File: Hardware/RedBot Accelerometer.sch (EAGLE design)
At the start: 18 parts, among them U1 MMA8452Q, U2 MIC5205-3.3V, U3 PCA9306

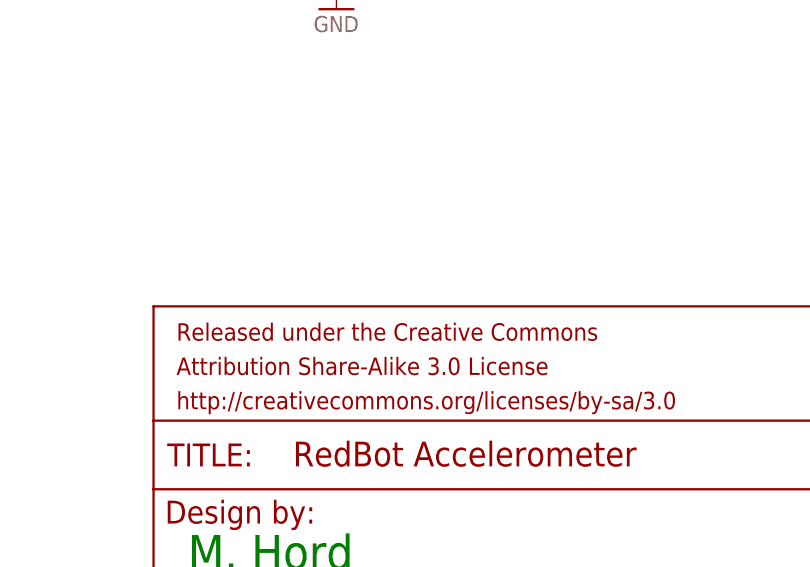
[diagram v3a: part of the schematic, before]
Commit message: added fiducials to board
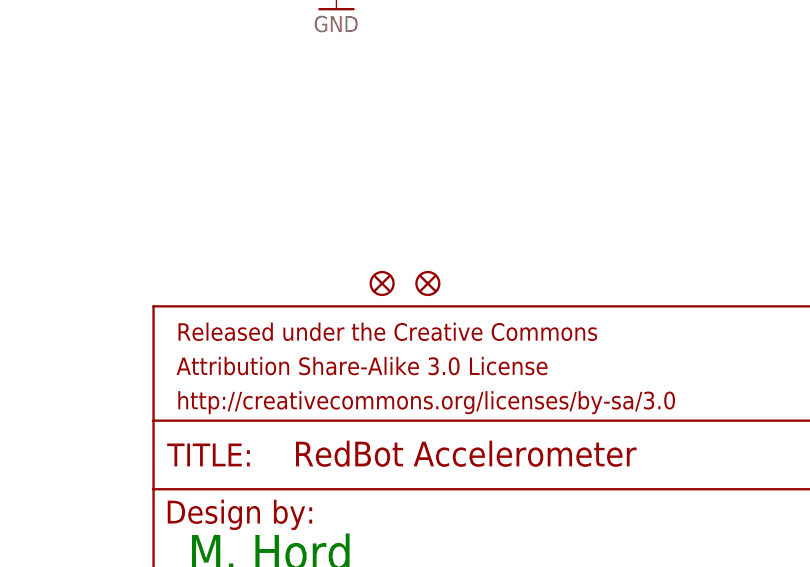
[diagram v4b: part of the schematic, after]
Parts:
- added FID1, FID2: FIDUCIALUFIDUCIAL, SparkFun-Aesthetics:FIDUCIALUFIDUCIAL
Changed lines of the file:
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@@
 <?xml version="1.0" encoding="utf-8"?>
 <!DOCTYPE eagle SYSTEM "eagle.dtd">
-<eagle version="6.4">
+<eagle version="6.5.0">
 <drawing>
 <settings>
@@
 <grid distance="0.1" unitdist="inch" unit="inch" style="lines" multiple="1" display="no" altdistance="0.01" altunitdist="inch" altunit="inch"/>
 <layers>
-<layer number="1" name="Top" color="4" fill="1" visible="yes" active="no"/>
-<layer number="2" name="Route2" color="1" fill="3" visible="yes" active="no"/>
-<layer number="3" name="Route3" color="4" fill="3" visible="yes" active="no"/>
-<layer number="4" name="Route4" color="1" fill="4" visible="yes" active="no"/>
-<layer number="5" name="Route5" color="4" fill="4" visible="yes" active="no"/>
-<layer number="6" name="Route6" color="1" fill="8" visible="yes" active="no"/>
-<layer number="7" name="Route7" color="4" fill="8" visible="yes" active="no"/>
-<layer number="8" name="Route8" color="1" fill="2" visible="yes" active="no"/>
-<layer number="9" name="Route9" color="4" fill="2" visible="yes" active="no"/>
-<layer number="10" name="Route10" color="1" fill="7" visible="yes" active="no"/>
-<layer number="11" name="Route11" color="4" fill="7" visible="yes" active="no"/>
-<layer number="12" name="Route12" color="1" fill="5" visible="yes" active="no"/>
-<layer number="13" name="Route13" color="4" fill="5" visible="yes" active="no"/>
-<layer number="14" name="Route14" color="1" fill="6" visible="yes" active="no"/>
-<layer number="15" name="Route15" color="4" fill="6" visible="yes" active="no"/>
-<layer number="16" name="Bottom" color="1" fill="1" visible="yes" active="no"/>
-<layer number="17" name="Pads" color="2" fill="1" visible="yes" active="no"/>
-<layer number="18" name="Vias" color="2" fill="1" visible="yes" active="no"/>
-<layer number="19" name="Unrouted" color="6" fill="1" visible="yes" active="no"/>
-<layer number="20" name="Dimension" color="15" fill="1" visible="yes" active="no"/>
-<layer number="21" name="tPlace" color="16" fill="1" visible="yes" active="no"/>
-<layer number="22" name="bPlace" color="14" fill="1" visible="yes" active="no"/>
-<layer number="23" name="tOrigins" color="15" fill="1" visible="yes" active="no"/>
-<layer number="24" name="bOrigins" color="15" fill="1" visible="yes" active="no"/>
-<layer number="25" name="tNames" color="7" fill="1" visible="yes" active="no"/>
-<layer number="26" name="bNames" color="7" fill="1" visible="yes" active="no"/>
-<layer number="27" name="tValues" color="7" fill="1" visible="yes" active="no"/>
-<layer number="28" name="bValues" color="7" fill="1" visible="yes" active="no"/>
+<layer number="1" name="Top" color="4" fill="1" visible="no" active="no"/>
+<layer number="2" name="Route2" color="1" fill="3" visible="no" active="no"/>
+<layer number="3" name="Route3" color="4" fill="3" visible="no" active="no"/>
+<layer number="4" name="Route4" color="1" fill="4" visible="no" active="no"/>
+<layer number="5" name="Route5" color="4" fill="4" visible="no" active="no"/>
+<layer number="6" name="Route6" color="1" fill="8" visible="no" active="no"/>
+<layer number="7" name="Route7" color="4" fill="8" visible="no" active="no"/>
+<layer number="8" name="Route8" color="1" fill="2" visible="no" active="no"/>
+<layer number="9" name="Route9" color="4" fill="2" visible="no" active="no"/>
+<layer number="10" name="Route10" color="1" fill="7" visible="no" active="no"/>
+<layer number="11" name="Route11" color="4" fill="7" visible="no" active="no"/>
+<layer number="12" name="Route12" color="1" fill="5" visible="no" active="no"/>
+<layer number="13" name="Route13" color="4" fill="5" visible="no" active="no"/>
+<layer number="14" name="Route14" color="1" fill="6" visible="no" active="no"/>
+<layer number="15" name="Route15" color="4" fill="6" visible="no" active="no"/>
+<layer number="16" name="Bottom" color="1" fill="1" visible="no" active="no"/>
+<layer number="17" name="Pads" color="2" fill="1" visible="no" active="no"/>
+<layer number="18" name="Vias" color="2" fill="1" visible="no" active="no"/>
+<layer number="19" name="Unrouted" color="6" fill="1" visible="no" active="no"/>
+<layer number="20" name="Dimension" color="15" fill="1" visible="no" active="no"/>
+<layer number="21" name="tPlace" color="16" fill="1" visible="no" active="no"/>
+<layer number="22" name="bPlace" color="14" fill="1" visible="no" active="no"/>
+<layer number="23" name="tOrigins" color="15" fill="1" visible="no" active="no"/>
+<layer number="24" name="bOrigins" color="15" fill="1" visible="no" active="no"/>
+<layer number="25" name="tNames" color="7" fill="1" visible="no" active="no"/>
+<layer number="26" name="bNames" color="7" fill="1" visible="no" active="no"/>
+<layer number="27" name="tValues" color="7" fill="1" visible="no" active="no"/>
+<layer number="28" name="bValues" color="7" fill="1" visible="no" active="no"/>
 <layer number="29" name="tStop" color="7" fill="3" visible="no" active="no"/>
 <layer number="30" name="bStop" color="7" fill="6" visible="no" active="no"/>
@@
 <layer number="35" name="tGlue" color="7" fill="4" visible="no" active="no"/>
 <layer number="36" name="bGlue" color="7" fill="5" visible="no" active="no"/>
-<layer number="37" name="tTest" color="7" fill="1" visible="yes" active="no"/>
-<layer number="38" name="bTest" color="7" fill="1" visible="yes" active="no"/>
+<layer number="37" name="tTest" color="7" fill="1" visible="no" active="no"/>
+<layer number="38" name="bTest" color="7" fill="1" visible="no" active="no"/>
 <layer number="39" name="tKeepout" color="4" fill="11" visible="no" active="no"/>
 <layer number="40" name="bKeepout" color="1" fill="11" visible="no" active="no"/>
@@
 <layer number="44" name="Drills" color="7" fill="1" visible="no" active="no"/>
 <layer number="45" name="Holes" color="7" fill="1" visible="no" active="no"/>
-<layer number="46" name="Milling" color="3" fill="1" visible="yes" active="no"/>
-<layer number="47" name="Measures" color="7" fill="1" visible="yes" active="no"/>
-<layer number="48" name="Document" color="7" fill="1" visible="yes" active="no"/>
-<layer number="49" name="Reference" color="7" fill="1" visible="yes" active="no"/>
-<layer number="50" name="dxf" color="7" fill="1" visible="yes" active="no"/>
-<layer number="51" name="tDocu" color="6" fill="1" visible="yes" active="no"/>
-<layer number="52" name="bDocu" color="7" fill="1" visible="yes" active="no"/>
-<layer number="53" name="tGND_GNDA" color="7" fill="9" visible="yes" active="no"/>
-<layer number="54" name="bGND_GNDA" color="1" fill="9" visible="yes" active="no"/>
-<layer number="56" name="wert" color="7" fill="1" visible="yes" active="no"/>
+<layer number="46" name="Milling" color="3" fill="1" visible="no" active="no"/>
+<layer number="47" name="Measures" color="7" fill="1" visible="no" active="no"/>
+<layer number="48" name="Document" color="7" fill="1" visible="no" active="no"/>
+<layer number="49" name="Reference" color="7" fill="1" visible="no" active="no"/>
+<layer number="50" name="dxf" color="7" fill="1" visible="no" active="no"/>
+<layer number="51" name="tDocu" color="6" fill="1" visible="no" active="no"/>
+<layer number="52" name="bDocu" color="7" fill="1" visible="no" active="no"/>
+<layer number="53" name="tGND_GNDA" color="7" fill="9" visible="no" active="no"/>
+<layer number="54" name="bGND_GNDA" color="1" fill="9" visible="no" active="no"/>
+<layer number="56" name="wert" color="7" fill="1" visible="no" active="no"/>
 <layer number="91" name="Nets" color="2" fill="1" visible="yes" active="yes"/>
 <layer number="92" name="Busses" color="1" fill="1" visible="yes" active="yes"/>
@@
 <part name="GND6" library="SparkFun-Aesthetics" deviceset="GND" device=""/>
 <part name="SUPPLY8" library="SparkFun-Aesthetics" deviceset="5V" device=""/>
+<part name="FID1" library="SparkFun-Aesthetics" deviceset="FIDUCIAL" device="UFIDUCIAL"/>
+<part name="FID2" library="SparkFun-Aesthetics" deviceset="FIDUCIAL" device="UFIDUCIAL"/>
 </parts>
 <sheets>
@@
 <instance part="GND6" gate="1" x="210.82" y="111.76"/>
 <instance part="SUPPLY8" gate="G$1" x="210.82" y="137.16"/>
+<instance part="FID1" gate="G$1" x="172.72" y="38.1"/>
+<instance part="FID2" gate="G$1" x="177.8" y="38.1"/>
 </instances>
 <busses>

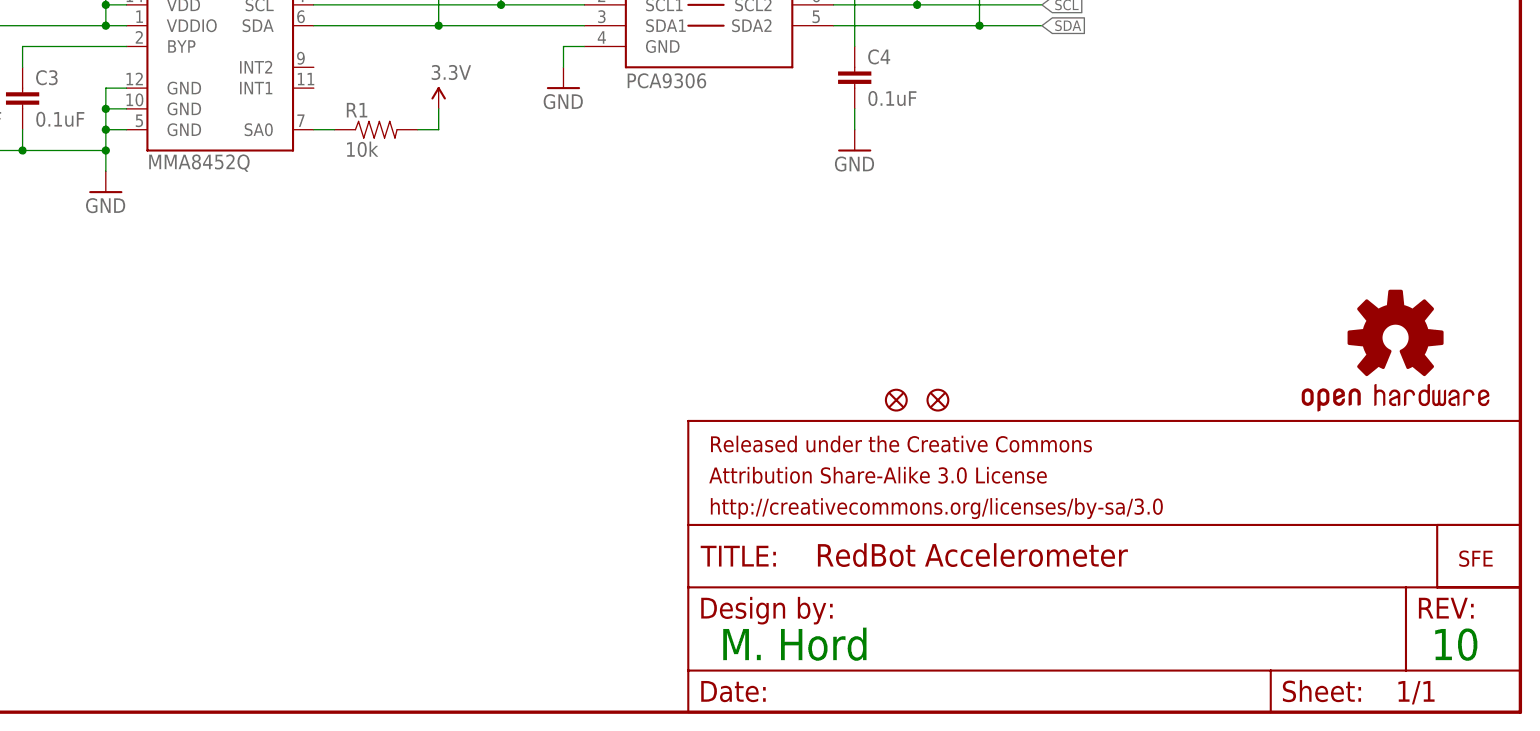
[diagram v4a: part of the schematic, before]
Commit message: Added 1:1 for PCA and Accel , 0603 update
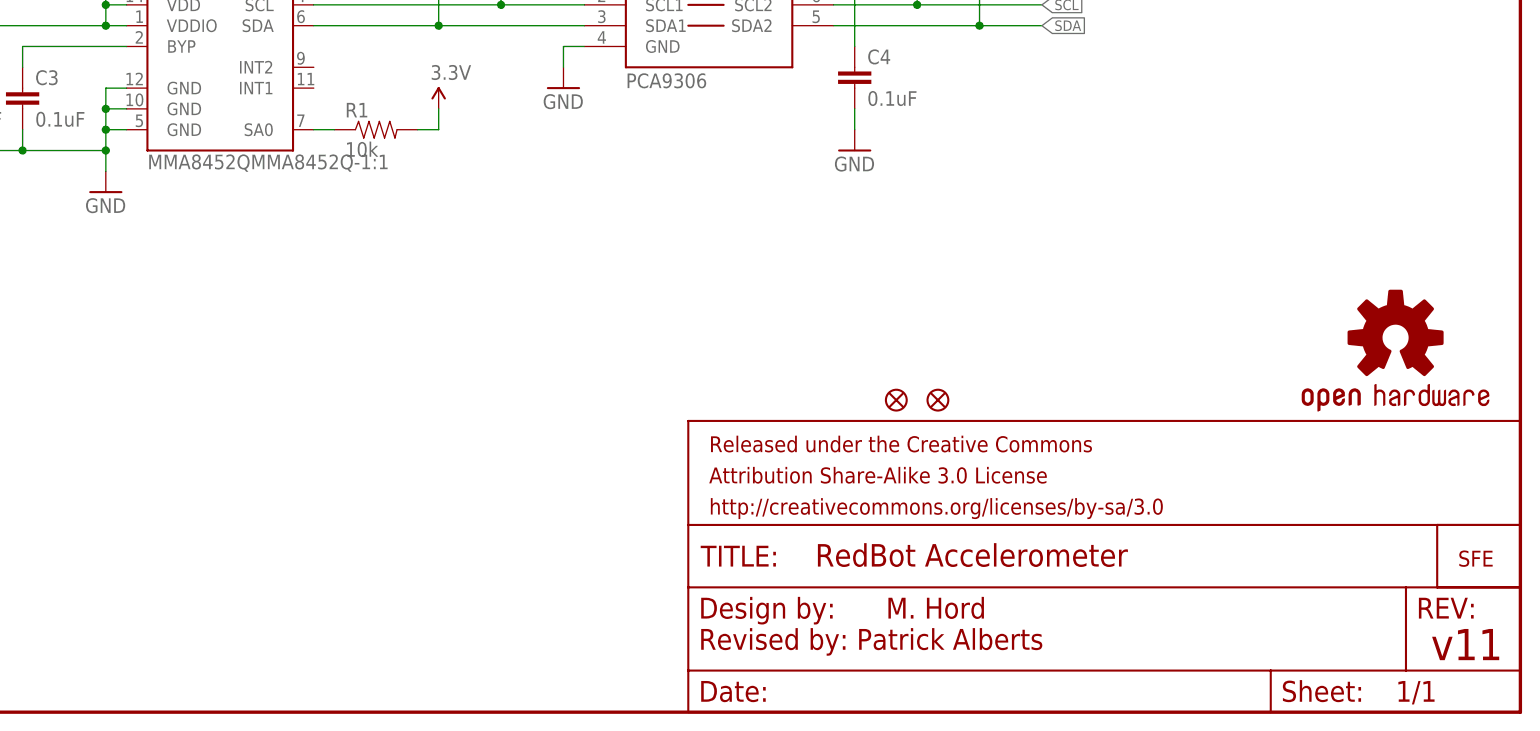
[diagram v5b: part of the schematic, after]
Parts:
- U1: value MMA8452Q -> MMA8452QMMA8452Q-1:1; device SparkFun-Sensors:MMA8452Q -> SparkFun-Sensors:MMA8452QMMA8452Q-1:1
- U3: device SparkFun-DigitalIC:PCA9306 -> SparkFun-DigitalIC:PCA9306PCA9306DC-1:1
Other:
- note added: "Revised by: Patrick Alberts"
- note added: "v11"
- note removed: "10"
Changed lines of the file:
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@@
 <?xml version="1.0" encoding="utf-8"?>
 <!DOCTYPE eagle SYSTEM "eagle.dtd">
-<eagle version="6.5.0">
+<eagle version="6.4">
 <drawing>
 <settings>
@@
 <layer number="54" name="bGND_GNDA" color="1" fill="9" visible="no" active="no"/>
 <layer number="56" name="wert" color="7" fill="1" visible="no" active="no"/>
+<layer number="57" name="tCAD" color="7" fill="1" visible="no" active="no"/>
 <layer number="91" name="Nets" color="2" fill="1" visible="yes" active="yes"/>
 <layer number="92" name="Busses" color="1" fill="1" visible="yes" active="yes"/>
@@
 <layer number="97" name="Info" color="7" fill="1" visible="yes" active="yes"/>
 <layer number="98" name="Guide" color="6" fill="1" visible="yes" active="yes"/>
+<layer number="99" name="SpiceOrder" color="7" fill="1" visible="yes" active="yes"/>
 <layer number="100" name="Muster" color="7" fill="1" visible="no" active="no"/>
 <layer number="101" name="Patch_Top" color="12" fill="4" visible="no" active="yes"/>
@@
 <layer number="108" name="tplace-old" color="10" fill="1" visible="yes" active="yes"/>
 <layer number="109" name="ref-old" color="11" fill="1" visible="yes" active="yes"/>
+<layer number="110" name="fp0" color="7" fill="1" visible="yes" active="yes"/>
+<layer number="111" name="LPC17xx" color="7" fill="1" visible="yes" active="yes"/>
+<layer number="112" name="tSilk" color="7" fill="1" visible="yes" active="yes"/>
+<layer number="113" name="IDFDebug" color="7" fill="1" visible="yes" active="yes"/>
 <layer number="116" name="Patch_BOT" color="9" fill="4" visible="no" active="yes"/>
 <layer number="121" name="_tsilk" color="7" fill="1" visible="no" active="yes"/>
 <layer number="122" name="_bsilk" color="7" fill="1" visible="no" active="yes"/>
+<layer number="123" name="tTestmark" color="7" fill="1" visible="yes" active="yes"/>
+<layer number="124" name="bTestmark" color="7" fill="1" visible="yes" active="yes"/>
 <layer number="125" name="_tNames" color="7" fill="1" visible="no" active="yes"/>
+<layer number="126" name="_bNames" color="7" fill="1" visible="yes" active="yes"/>
+<layer number="127" name="_tValues" color="7" fill="1" visible="yes" active="yes"/>
+<layer number="128" name="_bValues" color="7" fill="1" visible="yes" active="yes"/>
+<layer number="131" name="tAdjust" color="7" fill="1" visible="yes" active="yes"/>
+<layer number="132" name="bAdjust" color="7" fill="1" visible="yes" active="yes"/>
 <layer number="144" name="Drill_legend" color="7" fill="1" visible="no" active="yes"/>
+<layer number="150" name="Notes" color="7" fill="1" visible="yes" active="yes"/>
 <layer number="151" name="HeatSink" color="7" fill="1" visible="no" active="yes"/>
+<layer number="152" name="_bDocu" color="7" fill="1" visible="yes" active="yes"/>
+<layer number="153" name="FabDoc1" color="7" fill="1" visible="yes" active="yes"/>
+<layer number="154" name="FabDoc2" color="7" fill="1" visible="yes" active="yes"/>
+<layer number="155" name="FabDoc3" color="7" fill="1" visible="yes" active="yes"/>
 <layer number="199" name="Contour" color="7" fill="1" visible="no" active="yes"/>
 <layer number="200" name="200bmp" color="1" fill="10" visible="no" active="yes"/>
@@
 <layer number="223" name="223bmp" color="24" fill="1" visible="no" active="no"/>
 <layer number="224" name="224bmp" color="25" fill="1" visible="no" active="no"/>
+<layer number="248" name="Housing" color="7" fill="1" visible="yes" active="yes"/>
+<layer number="249" name="Edge" color="7" fill="1" visible="yes" active="yes"/>
 <layer number="250" name="Descript" color="3" fill="1" visible="no" active="no"/>
 <layer number="251" name="SMDround" color="12" fill="11" visible="no" active="no"/>
@@
 <part name="LOGO2" library="SparkFun-Aesthetics" deviceset="OSHW-LOGO" device="S"/>
 <part name="C1" library="SparkFun-Capacitors" deviceset="0.1UF-25V(+80/-20%)(0603)" device="" value="0.1uF"/>
-<part name="U3" library="SparkFun-DigitalIC" deviceset="PCA9306" device="" value="PCA9306"/>
-<part name="U1" library="SparkFun-Sensors" deviceset="MMA8452Q" device=""/>
+<part name="U3" library="SparkFun-DigitalIC" deviceset="PCA9306" device="PCA9306DC-1:1" value="PCA9306"/>
+<part name="U1" library="SparkFun-Sensors" deviceset="MMA8452Q" device="MMA8452Q-1:1" value="MMA8452QMMA8452Q-1:1"/>
 <part name="R1" library="SparkFun-Resistors" deviceset="10KOHM1/10W1%(0603)" device="0603" value="10k"/>
 <part name="C2" library="SparkFun-Capacitors" deviceset="4.7UF-6.3V-10%(0603)" device="0603" value="4.7uF"/>
@@
 <sheet>
 <plain>
-<text x="237.998" y="6.35" size="3.81" layer="91">10</text>
-<text x="151.13" y="6.35" size="3.81" layer="91">M. Hord</text>
+<text x="237.998" y="6.35" size="3.81" layer="94">v11</text>
+<text x="171.45" y="11.43" size="2.54" layer="94">M. Hord</text>
 <text x="236.22" y="157.48" size="1.27" layer="97">Top side
 connector-
@@
 connector-
 Female</text>
+<text x="148.59" y="7.62" size="2.54" layer="94">Revised by: Patrick Alberts</text>
 </plain>
 <instances>

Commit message: Fixing version numbers
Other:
- note added: "v12"
- note removed: "v11"
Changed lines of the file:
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@@
 <?xml version="1.0" encoding="utf-8"?>
 <!DOCTYPE eagle SYSTEM "eagle.dtd">
-<eagle version="6.4">
+<eagle version="6.6.0">
 <drawing>
 <settings>
@@
 <sheet>
 <plain>
-<text x="237.998" y="6.35" size="3.81" layer="94">v11</text>
+<text x="237.998" y="6.35" size="3.81" layer="94">v12</text>
 <text x="171.45" y="11.43" size="2.54" layer="94">M. Hord</text>
 <text x="236.22" y="157.48" size="1.27" layer="97">Top side
